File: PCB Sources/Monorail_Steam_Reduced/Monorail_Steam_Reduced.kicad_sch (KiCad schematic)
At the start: 130 parts, among them J1 Conn_01x02_Male, J2 Conn_01x02_Male, J3 Conn_01x02_Male, J6 USB_C_Receptacle_USB2.0, J8 Conn_01x04_Male, J9 Conn_01x03_Male, SW3 RotaryEncoder_Switch, U1 SRV05-4, U2 XC6206PxxxMR, U3 RP2040TR7, U4 W25Q128JVS, Y1 Crystal_GND24_Small

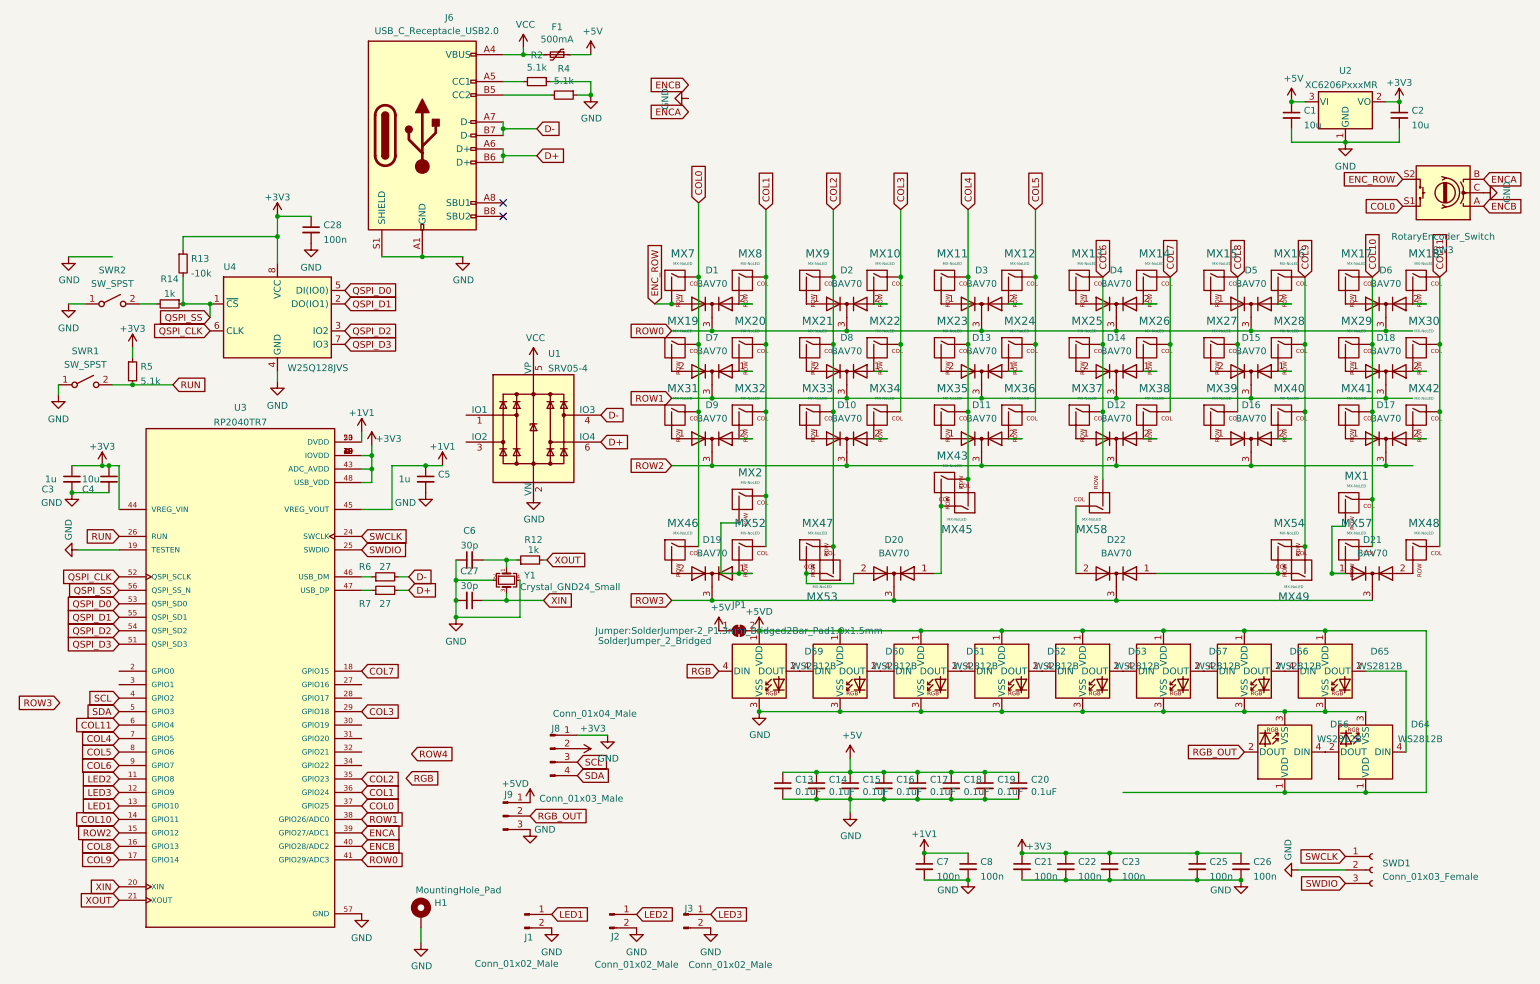
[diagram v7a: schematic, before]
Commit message: added silkscreen, finalized position and routing
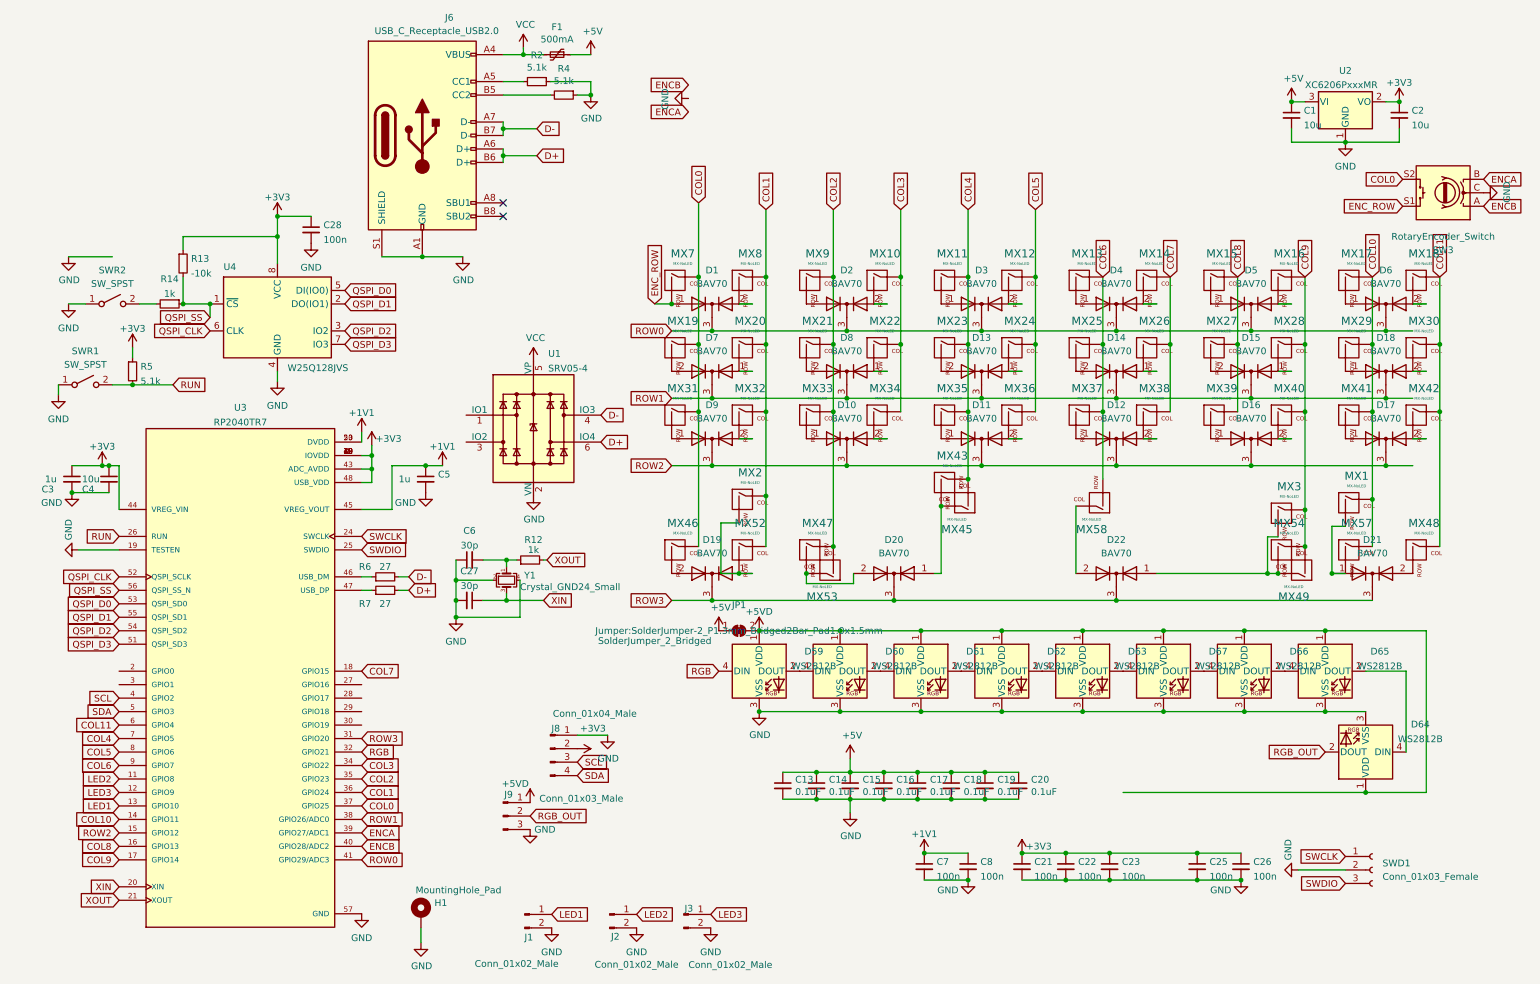
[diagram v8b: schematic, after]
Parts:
- removed D56: WS2812B, WS2812B:WS2812B_data-bridgeable, symbol LED:WS2812B
- added MX3: MX-NoLED, marbastlib-mx:SW_MX_1u, symbol MX_Alps_Hybrid:MX-NoLED
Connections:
- net COL0: now also SW3.S2; no longer SW3.S1
- net COL3: now also U3.34 (GPIO22); no longer U3.29 (GPIO18)
- net COL9: now also MX3.1 (COL)
- net ENC_ROW: now also SW3.S1; no longer SW3.S2
- net RGB: now also U3.32 (GPIO21)
- net RGB_OUT: now also D64.2 (DOUT)
- net ROW3: now also U3.31 (GPIO20)
- net at D22.1 (A), MX49.1 (COL), MX54.2 (ROW): now also MX3.2 (ROW)
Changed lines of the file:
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@@
   (junction (at 119.38 29.21) (diameter 0) (color 0 0 0 0)
   )
-  (junction (at 250.19 145.415) (diameter 0) (color 0 0 0 0)
-  )
   (junction (at 151.13 130.175) (diameter 0) (color 0 0 0 0)
   )
@@
   (junction (at 165.1 88.9) (diameter 0) (color 0 0 0 0)
   )
+  (junction (at 254 107.3912) (diameter 0) (color 0 0 0 0)
+  )
   (junction (at 193.04 73.66) (diameter 0) (color 0 0 0 0)
   )
@@
   (junction (at 187.325 156.845) (diameter 0) (color 0 0 0 0)
   )
+  (junction (at 246.9388 119.38) (diameter 0) (color 0 0 0 0)
+  )
   (junction (at 147.32 119.38) (diameter 0) (color 0 0 0 0)
   )
@@
   (junction (at 243.84 73.66) (diameter 0) (color 0 0 0 0)
   )
-  (junction (at 250.19 160.655) (diameter 0) (color 0 0 0 0)
-  )
   (junction (at 196.85 130.175) (diameter 0) (color 0 0 0 0)
   )
@@
   (no_connect (at 102.87 49.53))
   (no_connect (at 102.87 52.07))
+  (wire (pts (xy 246.9388 112.4712) (xy 246.9388 119.38))
+    (stroke (width 0) (type default))
+  )
   (wire (pts (xy 274.32 81.28) (xy 276.86 81.28))
     (stroke (width 0) (type default))
@@
     (stroke (width 0) (type default))
   )
+  (wire (pts (xy 226.06 119.38) (xy 246.9388 119.38))
+    (stroke (width 0) (type default))
+  )
   (wire (pts (xy 88.265 99.06) (xy 91.44 99.06))
     (stroke (width 0) (type default))
@@
     (stroke (width 0) (type default))
   )
+  (wire (pts (xy 254 107.3912) (xy 254 114.3))
+    (stroke (width 0) (type default))
+  )
   (wire (pts (xy 259.08 110.49) (xy 259.08 119.38))
     (stroke (width 0) (type default))
@@
     (stroke (width 0) (type default))
   )
-  (wire (pts (xy 219.71 160.655) (xy 250.19 160.655))
-    (stroke (width 0) (type default))
-  )
   (wire (pts (xy 184.15 119.38) (xy 185.42 119.38))
     (stroke (width 0) (type default))
   )
-  (wire (pts (xy 242.57 145.415) (xy 250.19 145.415))
-    (stroke (width 0) (type default))
-  )
   (wire (pts (xy 166.37 145.415) (xy 181.61 145.415))
     (stroke (width 0) (type default))
@@
     (stroke (width 0) (type default))
   )
+  (wire (pts (xy 246.9388 119.38) (xy 248.92 119.38))
+    (stroke (width 0) (type default))
+  )
   (wire (pts (xy 111.76 26.67) (xy 119.38 26.67))
     (stroke (width 0) (type default))
@@
     (stroke (width 0) (type default))
   )
-  (wire (pts (xy 226.06 119.38) (xy 248.92 119.38))
-    (stroke (width 0) (type default))
-  )
   (wire (pts (xy 190.5 88.9) (xy 190.5 101.6))
     (stroke (width 0) (type default))
@@
     (stroke (width 0) (type default))
   )
-  (wire (pts (xy 254 88.9) (xy 254 114.3))
+  (wire (pts (xy 254 88.9) (xy 254 107.3912))
+    (stroke (width 0) (type default))
+  )
+  (wire (pts (xy 248.92 112.4712) (xy 246.9388 112.4712))
     (stroke (width 0) (type default))
   )
@@
     (stroke (width 0) (type default))
   )
-  (wire (pts (xy 250.19 160.655) (xy 265.43 160.655))
+  (wire (pts (xy 219.71 160.655) (xy 265.43 160.655))
     (stroke (width 0) (type default))
   )
@@
     (stroke (width 0) (type default))
   )
-  (wire (pts (xy 250.19 145.415) (xy 257.81 145.415))
+  (wire (pts (xy 242.57 145.415) (xy 257.81 145.415))
     (stroke (width 0) (type default))
   )
@@
     )
   )
-  (global_label "COL0" (shape input) (at 272.415 50.165 180) (fields_autoplaced)
+  (global_label "COL0" (shape input) (at 272.415 45.085 180) (fields_autoplaced)
     (effects (font (size 1.27 1.27)) (justify right))
-    (property "Intersheetrefs" "${INTERSHEET_REFS}" (at 265.2459 50.165 0)
+    (property "Intersheetrefs" "${INTERSHEET_REFS}" (at 265.2459 45.085 0)
       (effects (font (size 1.27 1.27)) (justify right) hide)
     )
@@
     )
   )
-  (global_label "ROW3" (shape input) (at 19.304 143.764 180) (fields_autoplaced)
-    (effects (font (size 1.27 1.27)) (justify right))
-    (property "Intersheetrefs" "${INTERSHEET_REFS}" (at 11.7184 143.6846 0)
-      (effects (font (size 1.27 1.27)) (justify right) hide)
+  (global_label "ROW3" (shape input) (at 76.2 150.495 0) (fields_autoplaced)
+    (effects (font (size 1.27 1.27)) (justify left))
+    (property "Intersheetrefs" "${INTERSHEET_REFS}" (at 83.7924 150.495 0)
+      (effects (font (size 1.27 1.27)) (justify left) hide)
     )
   )
@@
     )
   )
-  (global_label "RGB" (shape input) (at 84.582 157.988 0) (fields_autoplaced)
+  (global_label "RGB" (shape input) (at 76.2 153.035 0) (fields_autoplaced)
     (effects (font (size 1.27 1.27)) (justify left))
-    (property "Intersheetrefs" "${INTERSHEET_REFS}" (at 90.7162 158.0674 0)
+    (property "Intersheetrefs" "${INTERSHEET_REFS}" (at 82.3342 153.1144 0)
       (effects (font (size 1.27 1.27)) (justify left) hide)
     )
@@
     )
   )
-  (global_label "ENC_ROW" (shape input) (at 272.415 45.085 180) (fields_autoplaced)
+  (global_label "ENC_ROW" (shape input) (at 272.415 50.165 180) (fields_autoplaced)
     (effects (font (size 1.27 1.27)) (justify right))
-    (property "Intersheetrefs" "${INTERSHEET_REFS}" (at 261.315 45.085 0)
+    (property "Intersheetrefs" "${INTERSHEET_REFS}" (at 261.315 50.165 0)
       (effects (font (size 1.27 1.27)) (justify right) hide)
     )
@@
     )
   )
-  (global_label "RGB_OUT" (shape input) (at 242.57 153.035 180) (fields_autoplaced)
+  (global_label "RGB_OUT" (shape input) (at 257.81 153.035 180) (fields_autoplaced)
     (effects (font (size 1.27 1.27)) (justify right))
-    (property "Intersheetrefs" "${INTERSHEET_REFS}" (at 231.8396 152.9556 0)
+    (property "Intersheetrefs" "${INTERSHEET_REFS}" (at 247.0796 152.9556 0)
       (effects (font (size 1.27 1.27)) (justify right) hide)
     )
@@
     )
   )
-  (global_label "ROW4" (shape input) (at 85.598 153.416 0) (fields_autoplaced)
-    (effects (font (size 1.27 1.27)) (justify left))
-    (property "Intersheetrefs" "${INTERSHEET_REFS}" (at 93.1836 153.3366 0)
-      (effects (font (size 1.27 1.27)) (justify left) hide)
-    )
-  )
-  (global_label "COL3" (shape input) (at 76.2 145.415 0) (fields_autoplaced)
+  (global_label "COL3" (shape input) (at 76.2 155.575 0) (fields_autoplaced)
     (effects (font (size 1.27 1.27)) (justify left))
-    (property "Intersheetrefs" "${INTERSHEET_REFS}" (at 83.3691 145.415 0)
+    (property "Intersheetrefs" "${INTERSHEET_REFS}" (at 83.3691 155.575 0)
       (effects (font (size 1.27 1.27)) (justify left) hide)
     )
@@
     )
   )
+  (symbol (lib_id "MX_Alps_Hybrid:MX-NoLED") (at 250.19 108.6612 0) (unit 1)
+    (in_bom yes) (on_board yes) (dnp no)
+    (property "Reference" "MX3" (at 251.0282 102.997 0)
+      (effects (font (size 1.524 1.524)))
+    )
+    (property "Value" "MX-NoLED" (at 251.0282 104.8766 0)
+      (effects (font (size 0.508 0.508)))
+    )
+    (property "Footprint" "marbastlib-mx:SW_MX_1u" (at 234.315 109.2962 0)
+      (effects (font (size 1.524 1.524)) hide)
+    )
+    (property "Datasheet" "" (at 234.315 109.2962 0)
+      (effects (font (size 1.524 1.524)) hide)
+    )
+    (pin "1")
+    (pin "2")
+    (instances
+      (project "Monorail_Steam_Reduced"
+        (path "/a3e4f0ae-9f86-49e9-b386-ed8b42e012fb"
+          (reference "MX3") (unit 1)
+        )
+      )
+    )
+  )
   (symbol (lib_id "LED:WS2812B") (at 257.81 137.795 0) (unit 1)
     (in_bom yes) (on_board yes) (dnp no) (fields_autoplaced)
@@
         )
       )
-    )
-  )
-  (symbol (lib_id "LED:WS2812B") (at 250.19 153.035 180) (unit 1)
-    (in_bom yes) (on_board yes) (dnp no) (fields_autoplaced)
-    (property "Reference" "D56" (at 260.4959 147.811 0)
-      (effects (font (size 1.27 1.27)))
-    )
-    (property "Value" "WS2812B" (at 260.4959 150.5861 0)
-      (effects (font (size 1.27 1.27)))
-    )
-    (property "Footprint" "WS2812B:WS2812B_data-bridgeable" (at 248.92 145.415 0)
-      (effects (font (size 1.27 1.27)) (justify left top) hide)
-    )
-    (property "Datasheet" "https://cdn-shop.adafruit.com/datasheets/WS2812B.pdf" (at 247.65 143.51 0)
-      (effects (font (size 1.27 1.27)) (justify left top) hide)
-    )
-    (pin "1")
-    (pin "2")
-    (pin "3")
-    (pin "4")
-    (instances
-      (project "Monorail_Steam_Reduced"
-        (path "/a3e4f0ae-9f86-49e9-b386-ed8b42e012fb"
-          (reference "D56") (unit 1)
-        )
-      )
